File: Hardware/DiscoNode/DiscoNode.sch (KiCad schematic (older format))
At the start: 68 parts, among them IC1 ATMEGA328PB-A, J1 1267, J2 RJ45, J3 RJ45, J4 AVR-ISP-6, J5 Debug, J6 0026605020, Q1 NTR4003N, Q2 NTR4003N, Q3 NTR4003N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

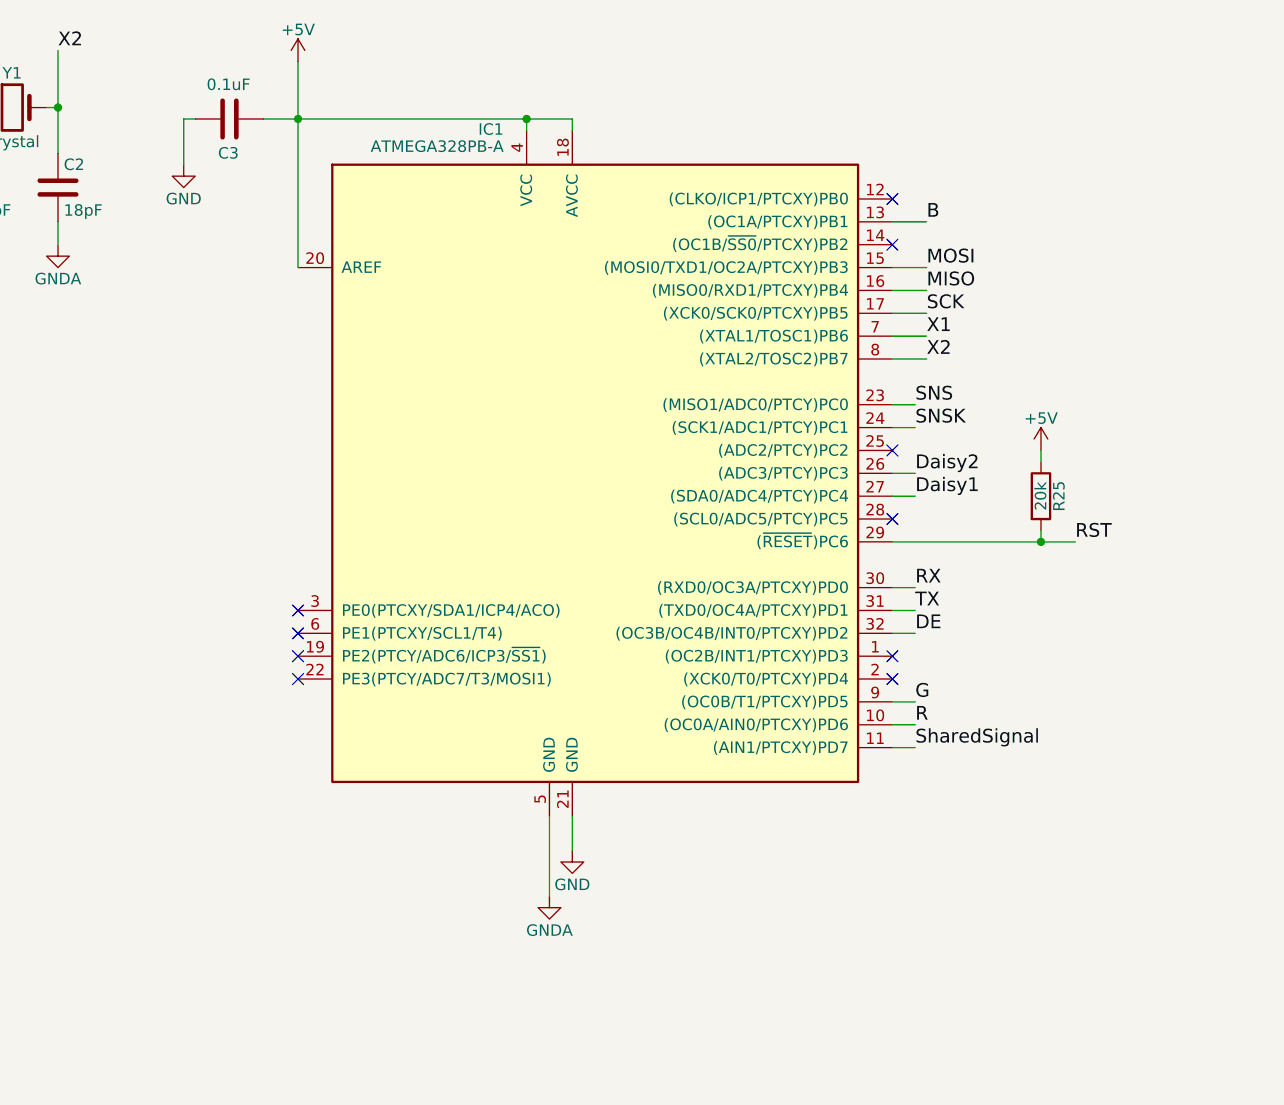
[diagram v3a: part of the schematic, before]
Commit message: Move parts around. Better LED layout. Move RJ45 jacks to edge of board
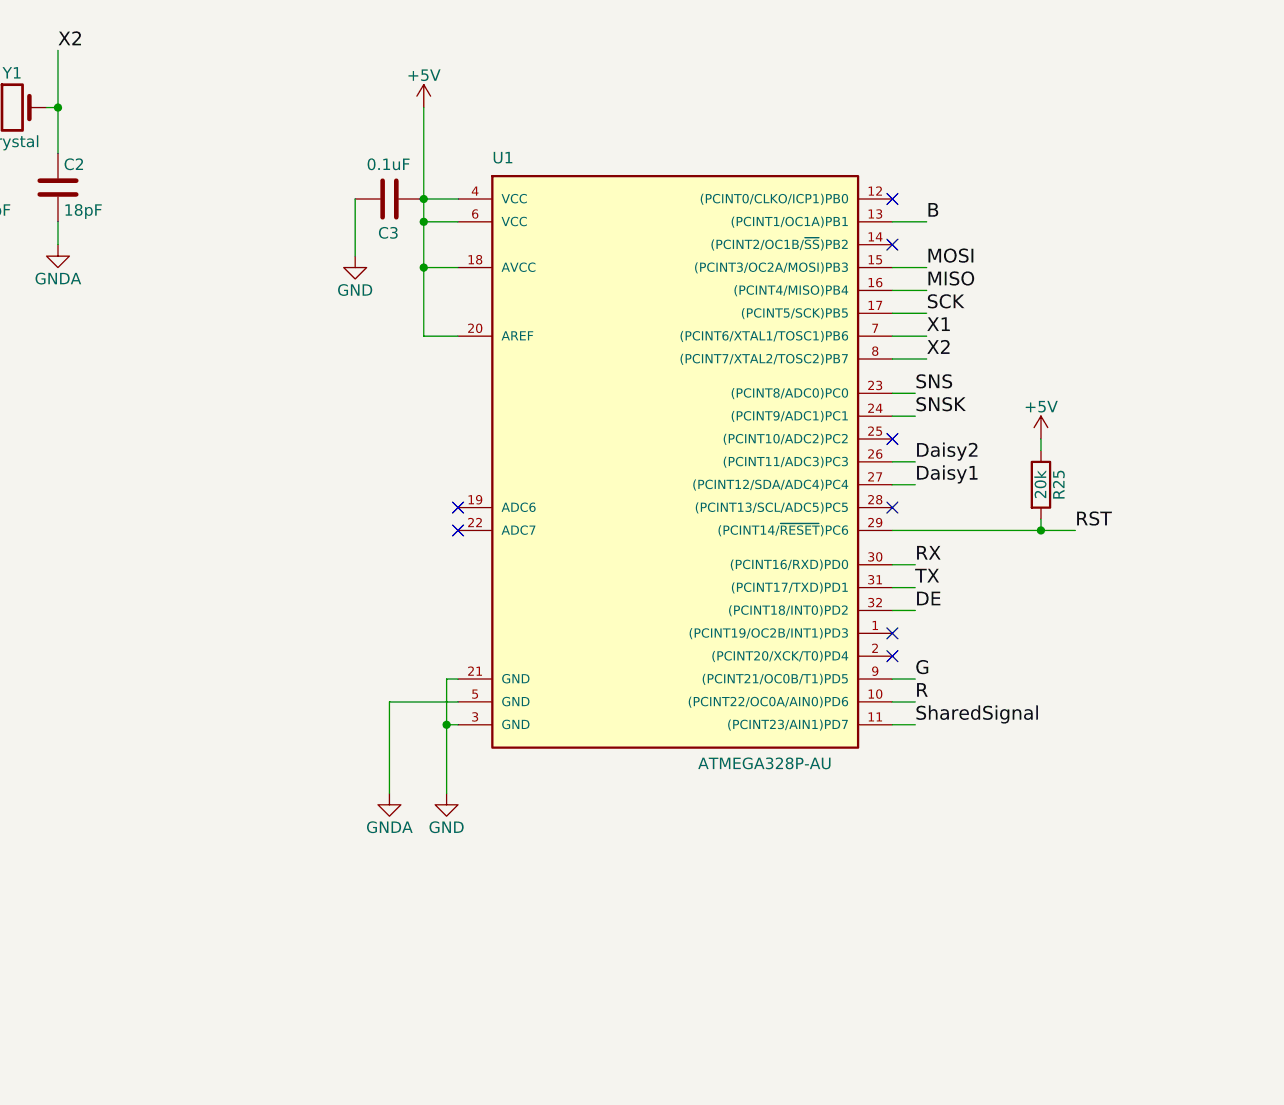
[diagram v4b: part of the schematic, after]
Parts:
- removed IC1: ATMEGA328PB-A, Housings_QFP:TQFP-32_7x7mm_Pitch0.8mm, symbol ATMEGA328PB-A
- added U1: ATMEGA328P-AU, TQFP32, symbol ATMEGA328P-AU
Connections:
- net +5V: now also U1.18 (AVCC), U1.20 (AREF), U1.4 (VCC), U1.6 (VCC)
- net B: now also U1.13 ((PCINT1/OC1A)PB1)
- net DE: now also U1.32 ((PCINT18/INT0)PD2)
- net Daisy1: now also U1.27 ((PCINT12/SDA/ADC4)PC4)
- net Daisy2: now also U1.26 ((PCINT11/ADC3)PC3)
- net G: now also U1.9 ((PCINT21/OC0B/T1)PD5)
- net GND: now also U1.21 (GND), U1.3 (GND)
- net GNDA: now also U1.5 (GND)
- net MISO: now also U1.16 ((PCINT4/MISO)PB4)
- net MOSI: now also U1.15 ((PCINT3/OC2A/MOSI)PB3)
- net R: now also U1.10 ((PCINT22/OC0A/AIN0)PD6)
- net RST: now also U1.29 ((PCINT14/~RESET~)PC6)
- net RX: now also U1.30 ((PCINT16/RXD)PD0)
- net SCK: now also U1.17 ((PCINT5/SCK)PB5)
- net SNS: now also U1.23 ((PCINT8/ADC0)PC0)
- net SNSK: now also U1.24 ((PCINT9/ADC1)PC1)
- net SharedSignal: now also U1.11 ((PCINT23/AIN1)PD7)
- net TX: now also U1.31 ((PCINT17/TXD)PD1)
- net X1: now also U1.7 ((PCINT6/XTAL1/TOSC1)PB6)
- net X2: now also U1.8 ((PCINT7/XTAL2/TOSC2)PB7)
- no-connect marks 12 -> 10
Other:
- moved on the sheet: C3, R25
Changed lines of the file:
@@
 	1    0    0    -1
 $EndComp
-Text Label 5150 2500 0    60   ~ 0
+Text Label 5150 2450 0    60   ~ 0
 SNS
-Text Label 5150 2600 0    60   ~ 0
+Text Label 5150 2550 0    60   ~ 0
 SNSK
 $Comp
@@
 	1    0    0    -1
 $EndComp
+Text Label 5150 3200 0    60   ~ 0
+RX
 Text Label 5150 3300 0    60   ~ 0
-RX
+TX
 Text Label 5150 3400 0    60   ~ 0
-TX
-Text Label 5150 3500 0    60   ~ 0
 DE
 $Comp
@@
 	1    0    0    -1
 $EndComp
-Text Label 5150 2800 0    60   ~ 0
+Text Label 5150 2750 0    60   ~ 0
 Daisy2
-Text Label 5150 2900 0    60   ~ 0
+Text Label 5150 2850 0    60   ~ 0
 Daisy1
-Text Label 5150 4000 0    60   ~ 0
+Text Label 5150 3900 0    60   ~ 0
 SharedSignal
-Text Label 5150 3900 0    60   ~ 0
+Text Label 5150 3800 0    60   ~ 0
 R
-Text Label 5150 3800 0    60   ~ 0
+Text Label 5150 3700 0    60   ~ 0
 G
 Text Label 5200 1900 0    60   ~ 0
@@
 L +5V #PWR014
 U 1 1 58C30CF6
-P 2450 1000
-F 0 "#PWR014" H 2450 850 50  0001 C CNN
-F 1 "+5V" H 2450 1140 50  0000 C CNN
-F 2 "" H 2450 1000 50  0000 C CNN
-F 3 "" H 2450 1000 50  0000 C CNN
-	1    2450 1000
-	1    0    0    -1
-$EndComp
-Text Label 5850 3100 0    60   ~ 0
+P 3000 1200
+F 0 "#PWR014" H 3000 1050 50  0001 C CNN
+F 1 "+5V" H 3000 1340 50  0000 C CNN
+F 2 "" H 3000 1200 50  0000 C CNN
+F 3 "" H 3000 1200 50  0000 C CNN
+	1    3000 1200
+	1    0    0    -1
+$EndComp
+Text Label 5850 3050 0    60   ~ 0
 RST
 $Comp
 L +5V #PWR015
 U 1 1 58C31DD7
-P 5700 2700
-F 0 "#PWR015" H 5700 2550 50  0001 C CNN
-F 1 "+5V" H 5700 2840 50  0000 C CNN
-F 2 "" H 5700 2700 50  0000 C CNN
-F 3 "" H 5700 2700 50  0000 C CNN
-	1    5700 2700
+P 5700 2650
+F 0 "#PWR015" H 5700 2500 50  0001 C CNN
+F 1 "+5V" H 5700 2790 50  0000 C CNN
+F 2 "" H 5700 2650 50  0000 C CNN
+F 3 "" H 5700 2650 50  0000 C CNN
+	1    5700 2650
 	1    0    0    -1
 $EndComp
@@
 L R R25
 U 1 1 58C31E42
-P 5700 2900
-F 0 "R25" V 5780 2900 50  0000 C CNN
-F 1 "20k" V 5700 2900 50  0000 C CNN
-F 2 "Resistors_SMD:R_0805" V 5630 2900 50  0001 C CNN
-F 3 "" H 5700 2900 50  0000 C CNN
-F 4 "RMCF0805JT20K0" H 5700 2900 60  0001 C CNN "MPN"
-F 5 "RMCF0805JT20K0CT-ND" H 5700 2900 60  0001 C CNN "Digikey"
-	1    5700 2900
+P 5700 2850
+F 0 "R25" V 5780 2850 50  0000 C CNN
+F 1 "20k" V 5700 2850 50  0000 C CNN
+F 2 "Resistors_SMD:R_0805" V 5630 2850 50  0001 C CNN
+F 3 "" H 5700 2850 50  0000 C CNN
+F 4 "RMCF0805JT20K0" H 5700 2850 60  0001 C CNN "MPN"
+F 5 "RMCF0805JT20K0CT-ND" H 5700 2850 60  0001 C CNN "Digikey"
+	1    5700 2850
 	1    0    0    -1
 $EndComp
@@
 L C C3
 U 1 1 58C3249F
-P 2150 1250
-F 0 "C3" V 2300 1200 50  0000 L CNN
-F 1 "0.1uF" V 2000 1150 50  0000 L CNN
-F 2 "Capacitors_SMD:C_0805" H 2188 1100 50  0001 C CNN
-F 3 "" H 2150 1250 50  0000 C CNN
-F 4 "CL21F104ZAANNNC" H 2150 1250 60  0001 C CNN "MPN"
-F 5 "1276-1286-1-ND" H 2150 1250 60  0001 C CNN "Digikey"
-	1    2150 1250
+P 2850 1600
+F 0 "C3" V 3000 1550 50  0000 L CNN
+F 1 "0.1uF" V 2700 1500 50  0000 L CNN
+F 2 "Capacitors_SMD:C_0805" H 2888 1450 50  0001 C CNN
+F 3 "" H 2850 1600 50  0000 C CNN
+F 4 "CL21F104ZAANNNC" H 2850 1600 60  0001 C CNN "MPN"
+F 5 "1276-1286-1-ND" H 2850 1600 60  0001 C CNN "Digikey"
+	1    2850 1600
 	0    1    1    0
 $EndComp
@@
 L GND #PWR016
 U 1 1 58C327DA
-P 1950 1450
-F 0 "#PWR016" H 1950 1200 50  0001 C CNN
-F 1 "GND" H 1950 1300 50  0000 C CNN
-F 2 "" H 1950 1450 50  0000 C CNN
-F 3 "" H 1950 1450 50  0000 C CNN
-	1    1950 1450
+P 2700 1850
+F 0 "#PWR016" H 2700 1600 50  0001 C CNN
+F 1 "GND" H 2700 1700 50  0000 C CNN
+F 2 "" H 2700 1850 50  0000 C CNN
+F 3 "" H 2700 1850 50  0000 C CNN
+	1    2700 1850
 	1    0    0    -1
 $EndComp
@@
 $EndComp
 $Comp
-L ATMEGA328PB-A IC1
-U 1 1 58F3EAA2
-P 3750 2800
-F 0 "IC1" H 3350 4275 50  0000 R BNN
-F 1 "ATMEGA328PB-A" H 3350 4200 50  0000 R BNN
-F 2 "Housings_QFP:TQFP-32_7x7mm_Pitch0.8mm" H 3700 1400 50  0001 L CIN
-F 3 "" H 3450 2850 50  0000 C CNN
-	1    3750 2800
-	1    0    0    -1
-$EndComp
-$Comp
 L GND #PWR028
 U 1 1 58F42322
-P 3650 4450
-F 0 "#PWR028" H 3650 4200 50  0001 C CNN
-F 1 "GND" H 3650 4300 50  0000 C CNN
-F 2 "" H 3650 4450 50  0000 C CNN
-F 3 "" H 3650 4450 50  0000 C CNN
-	1    3650 4450
+P 3100 4200
+F 0 "#PWR028" H 3100 3950 50  0001 C CNN
+F 1 "GND" H 3100 4050 50  0000 C CNN
+F 2 "" H 3100 4200 50  0000 C CNN
+F 3 "" H 3100 4200 50  0000 C CNN
+	1    3100 4200
 	1    0    0    -1
 $EndComp
 Text Label 5200 1700 0    60   ~ 0
 B
+NoConn ~ 5050 3500
 NoConn ~ 5050 3600
-NoConn ~ 5050 3700
-NoConn ~ 5050 3000
+NoConn ~ 5050 2950
 NoConn ~ 5050 1800
 NoConn ~ 5050 1600
-NoConn ~ 2450 3400
-NoConn ~ 2450 3500
-NoConn ~ 2450 3600
-NoConn ~ 2450 3700
-NoConn ~ 5050 2700
+NoConn ~ 5050 2650
+$Comp
+L GNDA #PWR029
+U 1 1 58F41784
+P 2850 4200
+F 0 "#PWR029" H 2850 3950 50  0001 C CNN
+F 1 "GNDA" H 2850 4050 50  0000 C CNN
+F 2 "" H 2850 4200 50  0000 C CNN
+F 3 "" H 2850 4200 50  0000 C CNN
+	1    2850 4200
+	1    0    0    -1
+$EndComp
+$Comp
+L ATMEGA328P-AU U1
+U 1 1 5919154E
+P 4050 2700
+F 0 "U1" H 3300 3950 50  0000 L BNN
+F 1 "ATMEGA328P-AU" H 4200 1300 50  0000 L BNN
+F 2 "TQFP32" H 4050 2700 50  0001 C CIN
+F 3 "" H 4050 2700 50  0001 C CNN
+	1    4050 2700
+	1    0    0    -1
+$EndComp
 Wire Wire Line
 	4700 8200 4700 8650
@@
 	5050 1900 5200 1900
 Wire Wire Line
+	5050 3700 5150 3700
+Wire Wire Line
 	5050 3800 5150 3800
 Wire Wire Line
 	5050 3900 5150 3900
 Wire Wire Line
-	5050 4000 5150 4000
-Wire Wire Line
-	5050 2900 5150 2900
-Wire Wire Line
-	5150 2800 5050 2800
+	5050 2850 5150 2850
+Wire Wire Line
+	5150 2750 5050 2750
 Connection ~ 13450 2100
 Wire Wire Line
@@
 	8350 1950 8350 2000
 Wire Wire Line
-	5050 3500 5150 3500
-Wire Wire Line
-	5150 3400 5050 3400
-Wire Wire Line
-	5050 3300 5150 3300
+	5050 3400 5150 3400
+Wire Wire Line
+	5150 3300 5050 3300
+Wire Wire Line
+	5050 3200 5150 3200
 Connection ~ 7900 3000
 Wire Wire Line
@@
 	7350 4300 7650 4300
 Wire Wire Line
-	5150 2600 5050 2600
-Wire Wire Line
-	5050 2500 5150 2500
+	5150 2550 5050 2550
+Wire Wire Line
+	5050 2450 5150 2450
 Wire Wire Line
 	1400 1700 1400 1800
@@
 	1000 1200 1050 1200
 Wire Wire Line
-	5050 3100 5850 3100
-Wire Wire Line
-	1950 1450 1950 1250
-Wire Wire Line
-	1950 1250 2000 1250
+	5050 3050 5850 3050
 Wire Wire Line
 	13900 7050 13850 7050
@@
 Connection ~ 5100 10250
 Wire Wire Line
-	5700 2700 5700 2750
-Wire Wire Line
-	5700 3050 5700 3100
-Connection ~ 5700 3100
+	5700 2650 5700 2700
+Wire Wire Line
+	5700 3000 5700 3050
+Connection ~ 5700 3050
 Wire Wire Line
 	8800 9150 8850 9150
@@
 Connection ~ 10250 8200
 Wire Wire Line
-	2450 1000 2450 1900
-Wire Wire Line
-	3450 1250 3450 1300
-Connection ~ 3450 1250
-Wire Wire Line
-	2300 1250 3650 1250
-Connection ~ 2450 1250
-Wire Wire Line
 	5200 1700 5050 1700
 Wire Wire Line
-	3650 1250 3650 1300
-Wire Wire Line
 	5950 9050 5950 9100
 Wire Wire Line
@@
 	2150 9050 2150 9100
 Wire Wire Line
-	3650 4300 3650 4450
-$Comp
-L GNDA #PWR029
-U 1 1 58F41784
-P 3550 4650
-F 0 "#PWR029" H 3550 4400 50  0001 C CNN
-F 1 "GNDA" H 3550 4500 50  0000 C CNN
-F 2 "" H 3550 4650 50  0000 C CNN
-F 3 "" H 3550 4650 50  0000 C CNN
-	1    3550 4650
-	1    0    0    -1
-$EndComp
-Wire Wire Line
-	3550 4300 3550 4650
-Wire Wire Line
 	6350 9050 6350 9100
 Wire Wire Line
@@
 Wire Wire Line
 	3450 9800 3450 10250
+Wire Wire Line
+	3150 3700 3100 3700
+Wire Wire Line
+	3100 3700 3100 4200
+Wire Wire Line
+	3150 3900 3100 3900
+Connection ~ 3100 3900
+Wire Wire Line
+	3150 3800 2850 3800
+Wire Wire Line
+	2850 3800 2850 4200
+NoConn ~ 3150 3050
+NoConn ~ 3150 2950
+Wire Wire Line
+	3000 2200 3150 2200
+Wire Wire Line
+	3000 1200 3000 2200
+Wire Wire Line
+	3000 1600 3150 1600
+Wire Wire Line
+	3150 1700 3000 1700
+Connection ~ 3000 1700
+Wire Wire Line
+	3150 1900 3000 1900
+Connection ~ 3000 1900
+Wire Wire Line
+	2700 1600 2700 1850
+Connection ~ 3000 1600
 $EndSCHEMATC
